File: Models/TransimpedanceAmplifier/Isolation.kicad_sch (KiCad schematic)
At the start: 10 parts, among them U11 ISO7641FM, U12 ISO7641FM

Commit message: Starting major changes in response to the SOIC-8 version of OP37 being out of stock
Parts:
- U11, U12: Cost $0.00 -> $8.67; Cost (qty10) (none) -> $6.72; Purchase Link https://www.digikey.com/en/products/detail/texas-instrument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 -> https://www.mouser.com/ProductDetail/Texas-Instruments/ISO7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; RoHS Compliant NO -> YES
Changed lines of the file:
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@@
 			)
 		)
-		(property "Purchase Link" "https://www.digikey.com/en/products/detail/texas-instruments/ISO7641FMDWR/2799299"
+		(property "Purchase Link" "https://www.mouser.com/ProductDetail/Texas-Instruments/ISO7641FMDWR?qs=bhx7MkwkKU%252B3UeyY95zb0A%3D%3D"
 			(at 121.92 106.68 0)
 			(effects
@@
 			)
 		)
-		(property "Cost" "$0.00"
+		(property "Cost" "$8.67"
 			(at 121.92 106.68 0)
 			(effects
@@
 			)
 		)
-		(property "RoHS Compliant" "NO"
+		(property "RoHS Compliant" "YES"
+			(at 121.92 106.68 0)
+			(effects
+				(font
+					(size 1.27 1.27)
+				)
+				(hide yes)
+			)
+		)
+		(property "Cost (qty10)" "$6.72"
 			(at 121.92 106.68 0)
 			(effects
@@
 			)
 		)
-		(property "Purchase Link" "https://www.digikey.com/en/products/detail/texas-instruments/ISO7641FMDWR/2799299"
-			(at 121.92 45.72 0)
-			(effects
-				(font
-					(size 1.27 1.27)
-				)
-				(hide yes)
-			)
-		)
-		(property "Cost" "$0.00"
-			(at 121.92 45.72 0)
-			(effects
-				(font
-					(size 1.27 1.27)
-				)
-				(hide yes)
-			)
-		)
-		(property "RoHS Compliant" "NO"
-			(at 121.92 45.72 0)
-			(effects
+		(property "Purchase Link" "https://www.mouser.com/ProductDetail/Texas-Instruments/ISO7641FMDWR?qs=bhx7MkwkKU%252B3UeyY95zb0A%3D%3D"
+			(at 121.92 45.72 0)
+			(effects
+				(font
+					(size 1.27 1.27)
+				)
+				(hide yes)
+			)
+		)
+		(property "Cost" "$8.67"
+			(at 121.92 45.72 0)
+			(effects
+				(font
+					(size 1.27 1.27)
+				)
+				(hide yes)
+			)
+		)
+		(property "RoHS Compliant" "YES"
+			(at 121.92 45.72 0)
+			(effects
+				(font
+					(size 1.27 1.27)
+				)
+				(hide yes)
+			)
+		)
+		(property "Cost (qty10)" "$6.72"
+			(at 121.92 45.72 0)
+			(effects

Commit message: Patching up the bill of materials now
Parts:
- U11, U12: Cost $8.67 -> $0.00; Cost (qty10) $6.72 -> $0.00; Purchase Link https://www.mouser.com/ProductDetail/Texas-Instruments/ISO7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 -> (none)
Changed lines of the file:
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@@
 			)
 		)
-		(property "Purchase Link" "https://www.mouser.com/ProductDetail/Texas-Instruments/ISO7641FMDWR?qs=bhx7MkwkKU%252B3UeyY95zb0A%3D%3D"
+		(property "Purchase Link" ""
 			(at 121.92 106.68 0)
 			(effects
@@
 			)
 		)
-		(property "Cost" "$8.67"
+		(property "Cost" "$0.00"
 			(at 121.92 106.68 0)
 			(effects
@@
 			)
 		)
-		(property "Cost (qty10)" "$6.72"
+		(property "Cost (qty10)" "$0.00"
 			(at 121.92 106.68 0)
 			(effects
@@
 			)
 		)
-		(property "Purchase Link" "https://www.mouser.com/ProductDetail/Texas-Instruments/ISO7641FMDWR?qs=bhx7MkwkKU%252B3UeyY95zb0A%3D%3D"
-			(at 121.92 45.72 0)
-			(effects
-				(font
-					(size 1.27 1.27)
-				)
-				(hide yes)
-			)
-		)
-		(property "Cost" "$8.67"
+		(property "Purchase Link" ""
+			(at 121.92 45.72 0)
+			(effects
+				(font
+					(size 1.27 1.27)
+				)
+				(hide yes)
+			)
+		)
+		(property "Cost" "$0.00"
 			(at 121.92 45.72 0)
 			(effects
@@
 			)
 		)
-		(property "Cost (qty10)" "$6.72"
-			(at 121.92 45.72 0)
-			(effects
+		(property "Cost (qty10)" "$0.00"
+			(at 121.92 45.72 0)
+			(effects

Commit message: Exclude these pin headers from the BOM; they are just cheap breakaway pins
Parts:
- U11, U12: Cost $0.00 -> $8.62; Cost (qty10) $0.00 -> $6.695; Purchase Link (none) -> https://www.digikey.com/en/products/detail/texas-instrument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
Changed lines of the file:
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@@
 			)
 		)
-		(property "Purchase Link" ""
+		(property "Purchase Link" "https://www.digikey.com/en/products/detail/texas-instruments/ISO7641FMDWR/2799299"
 			(at 121.92 106.68 0)
 			(effects
@@
 			)
 		)
-		(property "Cost" "$0.00"
+		(property "Cost" "$8.62"
 			(at 121.92 106.68 0)
 			(effects
@@
 			)
 		)
-		(property "Cost (qty10)" "$0.00"
+		(property "Cost (qty10)" "$6.695"
 			(at 121.92 106.68 0)
 			(effects
@@
 			)
 		)
-		(property "Purchase Link" ""
-			(at 121.92 45.72 0)
-			(effects
-				(font
-					(size 1.27 1.27)
-				)
-				(hide yes)
-			)
-		)
-		(property "Cost" "$0.00"
+		(property "Purchase Link" "https://www.digikey.com/en/products/detail/texas-instruments/ISO7641FMDWR/2799299"
+			(at 121.92 45.72 0)
+			(effects
+				(font
+					(size 1.27 1.27)
+				)
+				(hide yes)
+			)
+		)
+		(property "Cost" "$8.62"
 			(at 121.92 45.72 0)
 			(effects
@@
 			)
 		)
-		(property "Cost (qty10)" "$0.00"
-			(at 121.92 45.72 0)
-			(effects
+		(property "Cost (qty10)" "$6.695"
+			(at 121.92 45.72 0)
+			(effects

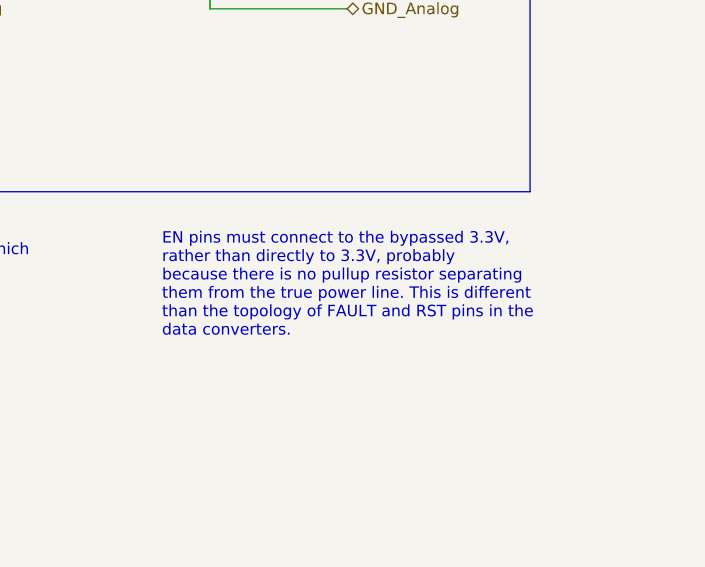
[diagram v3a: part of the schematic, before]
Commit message: Removed some complexity from the schematic while solving the layout problem
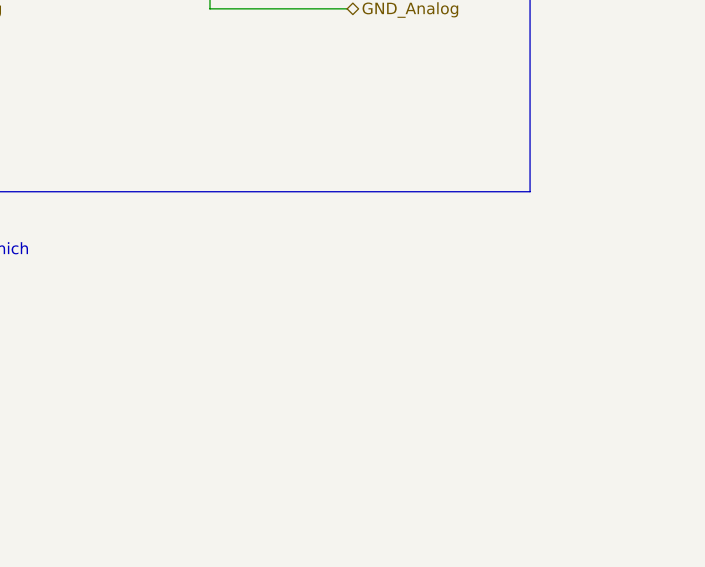
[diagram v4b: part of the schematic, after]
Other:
- note removed: "EN pins must connect to the bypassed 3.3V, rather than directly to 3.3V, probably because there is no pullup resistor separating them from the true power line. This is different than the topology of FAULT and RST pins in the data converters."
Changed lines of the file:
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@@
-		)
-	)
-	(text "EN pins must connect to the bypassed 3.3V,\nrather than directly to 3.3V, probably\nbecause there is no pullup resistor separating\nthem from the true power line. This is different\nthan the topology of FAULT and RST pins in the\ndata converters."
-		(exclude_from_sim no)
-		(at 213.106 149.352 0)
-		(effects
-			(font
-				(size 1.27 1.27)
-			)
-			(justify left top)
 		)
 	)

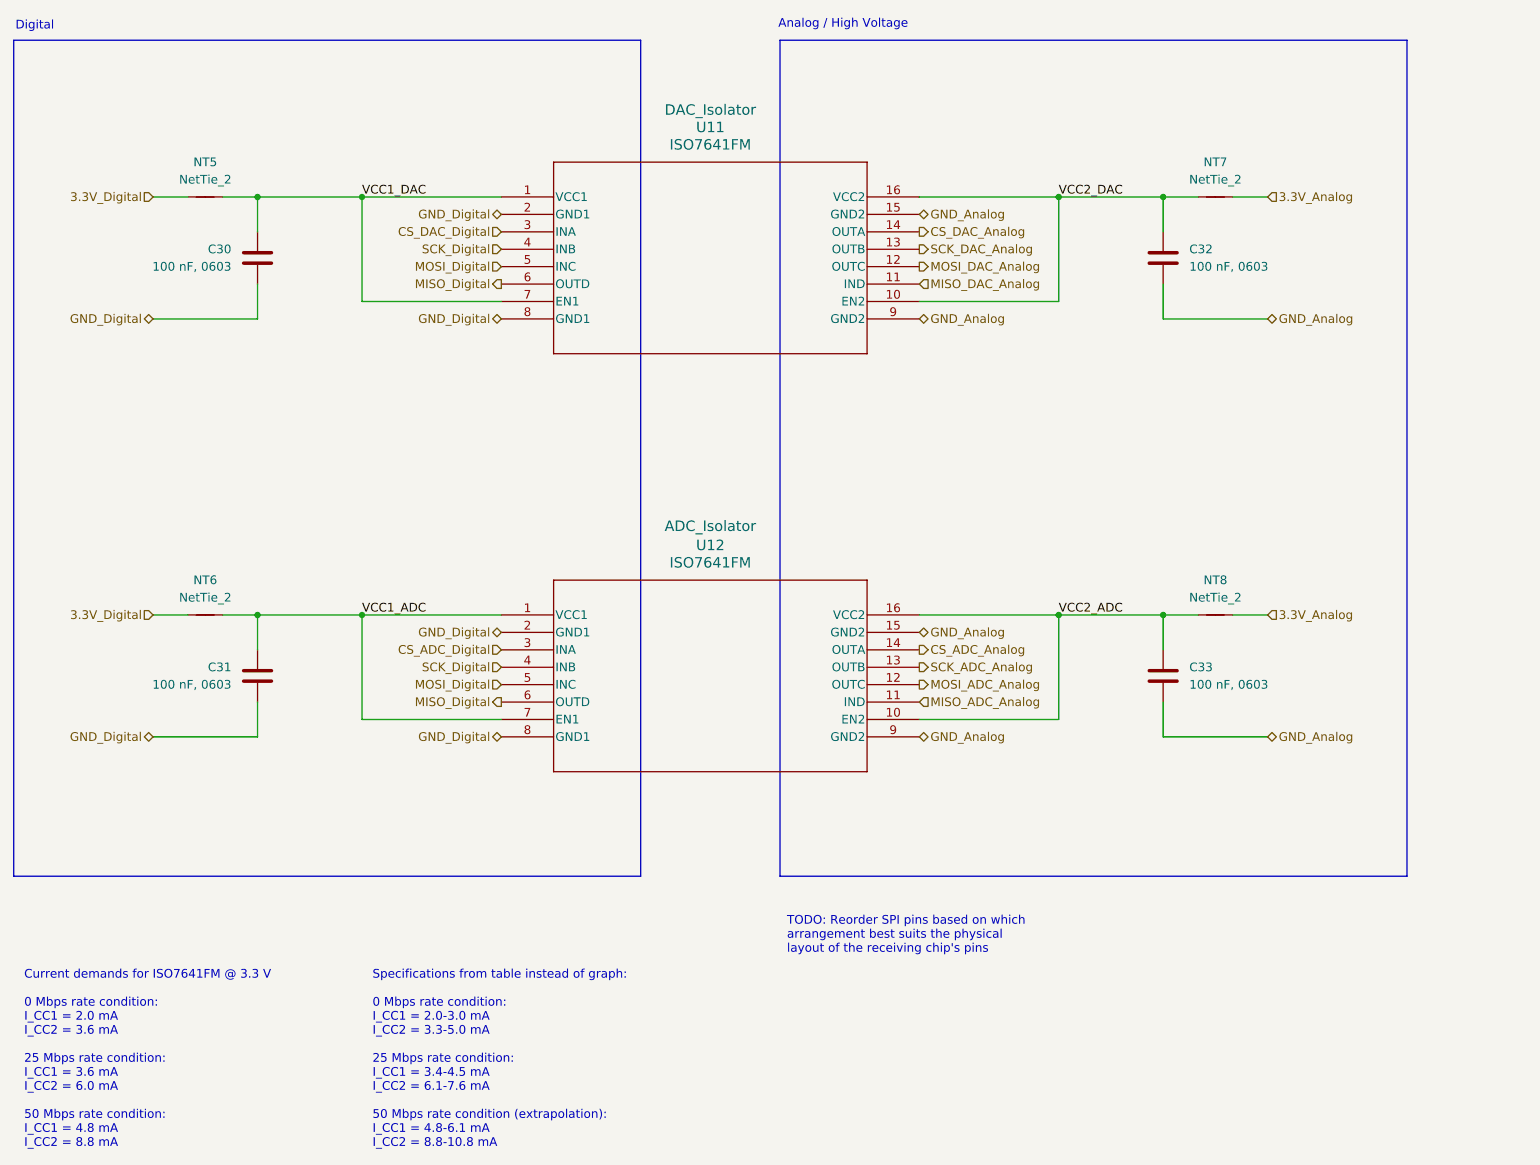
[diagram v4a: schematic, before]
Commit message: Patched the pin ordering of the isolators
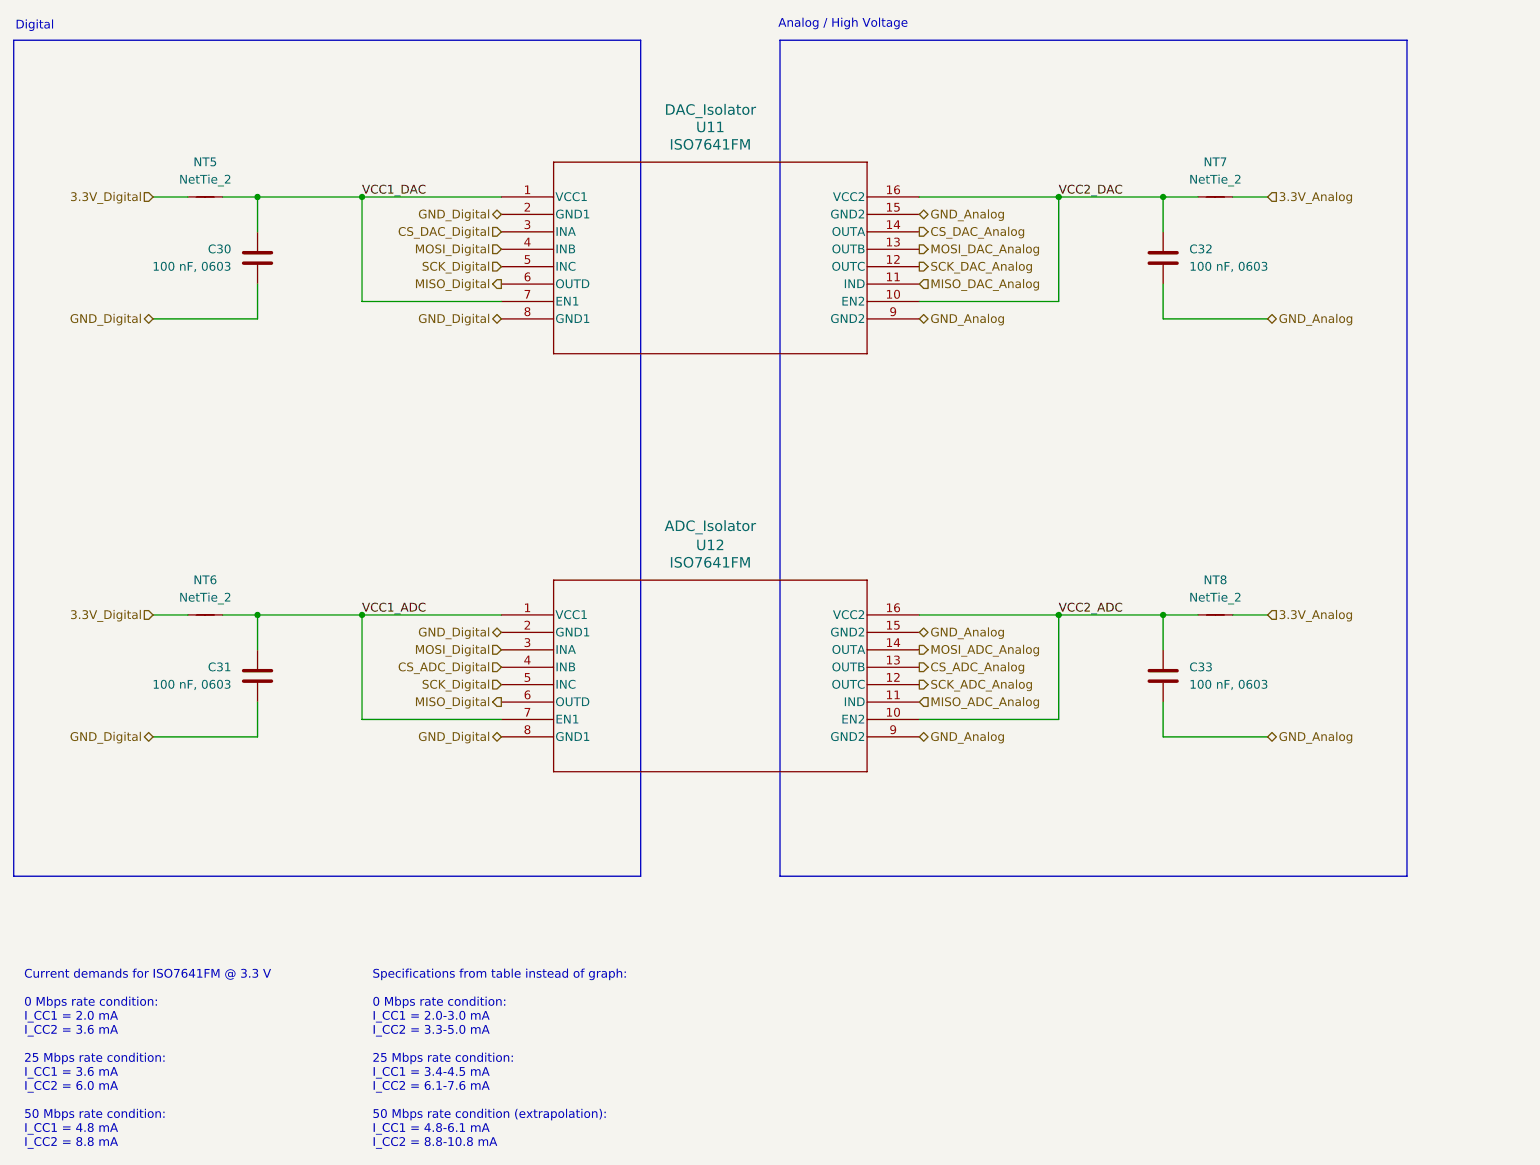
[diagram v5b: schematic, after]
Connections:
- net CS_ADC_Analog: now also U12.13 (OUTB); no longer U12.14 (OUTA)
- net CS_ADC_Digital: now also U12.4 (INB); no longer U12.3 (INA)
- net MOSI_ADC_Analog: now also U12.14 (OUTA); no longer U12.12 (OUTC)
- net MOSI_DAC_Analog: now also U11.13 (OUTB); no longer U11.12 (OUTC)
- net MOSI_Digital: now also U11.4 (INB), U12.3 (INA); no longer U11.5 (INC), U12.5 (INC)
- net SCK_ADC_Analog: now also U12.12 (OUTC); no longer U12.13 (OUTB)
- net SCK_DAC_Analog: now also U11.12 (OUTC); no longer U11.13 (OUTB)
- net SCK_Digital: now also U11.5 (INC), U12.5 (INC); no longer U11.4 (INB), U12.4 (INB)
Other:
- note removed: "TODO: Reorder SPI pins based on which arrangement best suits the physical layout of the receiving chip's pins"
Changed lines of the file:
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@@
-		)
-	)
-	(text "TODO: Reorder SPI pins based on which\narrangement best suits the physical\nlayout of the receiving chip's pins"
-		(exclude_from_sim no)
-		(at 163.576 153.416 0)
-		(effects
-			(font
-				(size 1.27 1.27)
-			)
-			(justify left)
 		)
 	)
@@
 	(hierarchical_label "SCK_Digital"
 		(shape input)
-		(at 121.92 53.34 180)
+		(at 121.92 55.88 180)
 		(effects
 			(font
@@
 	(hierarchical_label "CS_ADC_Analog"
 		(shape output)
-		(at 182.88 111.76 0)
+		(at 182.88 114.3 0)
 		(effects
 			(font
@@
 	(hierarchical_label "MOSI_ADC_Analog"
 		(shape output)
-		(at 182.88 116.84 0)
+		(at 182.88 111.76 0)
 		(effects
 			(font
@@
 	(hierarchical_label "MOSI_DAC_Analog"
 		(shape output)
-		(at 182.88 55.88 0)
+		(at 182.88 53.34 0)
 		(effects
 			(font
@@
 	(hierarchical_label "CS_ADC_Digital"
 		(shape input)
+		(at 121.92 114.3 180)
+		(effects
+			(font
+				(size 1.27 1.27)
+			)
+			(justify right)
+		)
+	)
+	(hierarchical_label "MOSI_Digital"
+		(shape input)
 		(at 121.92 111.76 180)
 		(effects
@@
 		)
 	)
-	(hierarchical_label "MOSI_Digital"
+	(hierarchical_label "3.3V_Analog"
+		(shape input)
+		(at 233.68 106.68 0)
+		(effects
+			(font
+				(size 1.27 1.27)
+			)
+			(justify left)
+		)
+	)
+	(hierarchical_label "SCK_Digital"
 		(shape input)
 		(at 121.92 116.84 180)
-		(effects
-			(font
-				(size 1.27 1.27)
-			)
-			(justify right)
-		)
-	)
-	(hierarchical_label "3.3V_Analog"
-		(shape input)
-		(at 233.68 106.68 0)
-		(effects
-			(font
-				(size 1.27 1.27)
-			)
-			(justify left)
-		)
-	)
-	(hierarchical_label "SCK_Digital"
-		(shape input)
-		(at 121.92 114.3 180)
 		(effects
 			(font
@@
 	(hierarchical_label "SCK_ADC_Analog"
 		(shape output)
-		(at 182.88 114.3 0)
+		(at 182.88 116.84 0)
 		(effects
 			(font
@@
 	(hierarchical_label "SCK_DAC_Analog"
 		(shape output)
-		(at 182.88 53.34 0)
+		(at 182.88 55.88 0)
 		(effects
 			(font
@@
 	(hierarchical_label "MOSI_Digital"
 		(shape input)
-		(at 121.92 55.88 180)
-		(effects
-			(font
+		(at 121.92 53.34 180)
+		(effects
+			(font
